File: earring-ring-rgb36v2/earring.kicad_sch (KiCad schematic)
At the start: 54 parts, among them J1 Conn_01x05, Q1 AO3401A, SW1 SW_Push, U2 STM32L031G6Ux

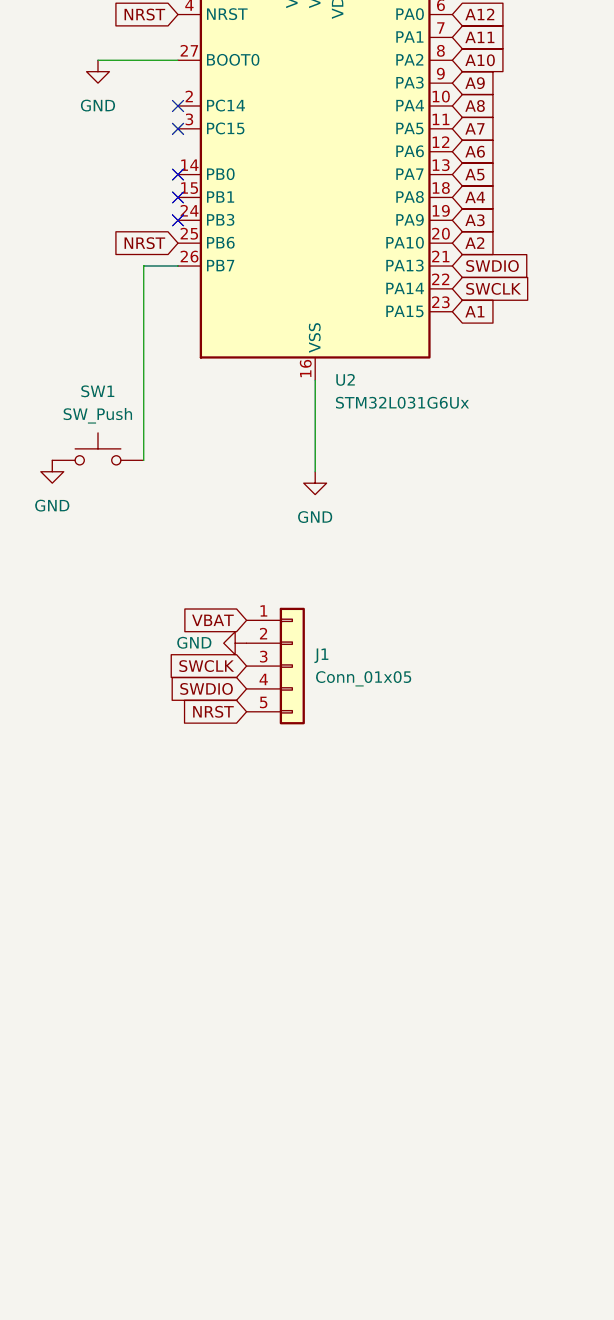
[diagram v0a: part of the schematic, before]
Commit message: earring-ring-rgb36v2: add phototransistor for light sensing
Can also be used for sending new programs, perhaps?
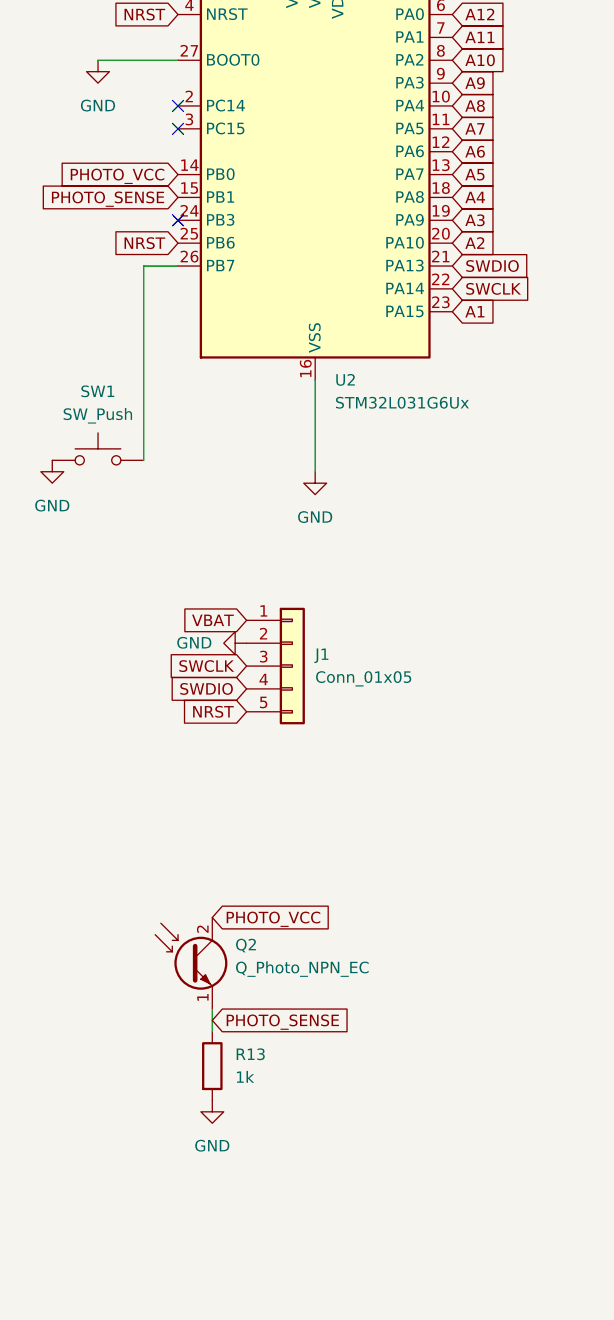
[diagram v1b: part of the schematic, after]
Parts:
- added Q2: Q_Photo_NPN_EC, Custom:Phototransistor_0603, symbol Device:Q_Photo_NPN_EC
- added R13: 1k, Resistor_SMD:R_0402_1005Metric, symbol Device:R
- J1: now left out of the parts list
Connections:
- net GND: now also R13.2
- net PHOTO_VCC: now reaches U2.14 (PB0)
- net PHOTO_VCC: now also Q2.2 (C)
- net PHOTO_SENSE: now reaches U2.15 (PB1)
- net PHOTO_SENSE: now also Q2.1 (E), R13.1
- no-connect marks 5 -> 3

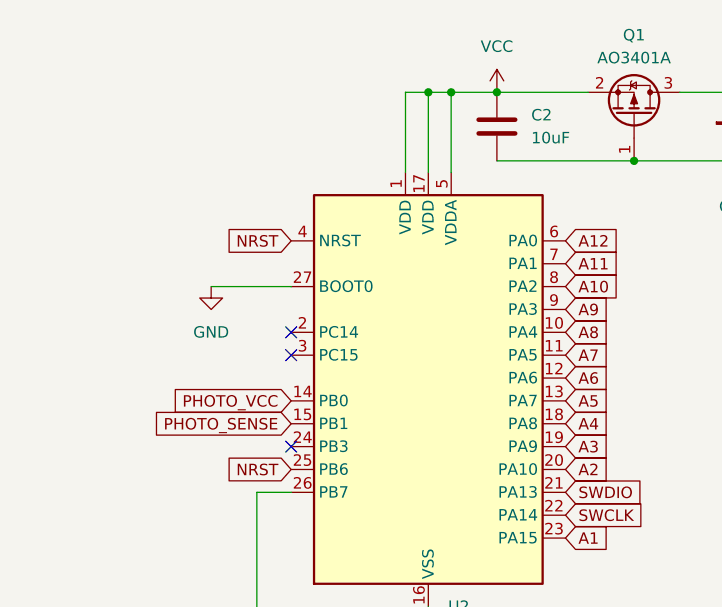
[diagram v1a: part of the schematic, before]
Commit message: earring-ring-rgb36v2: add 32768Hz crystal oscillator
No idea whether this is correct, might need some additional checking.
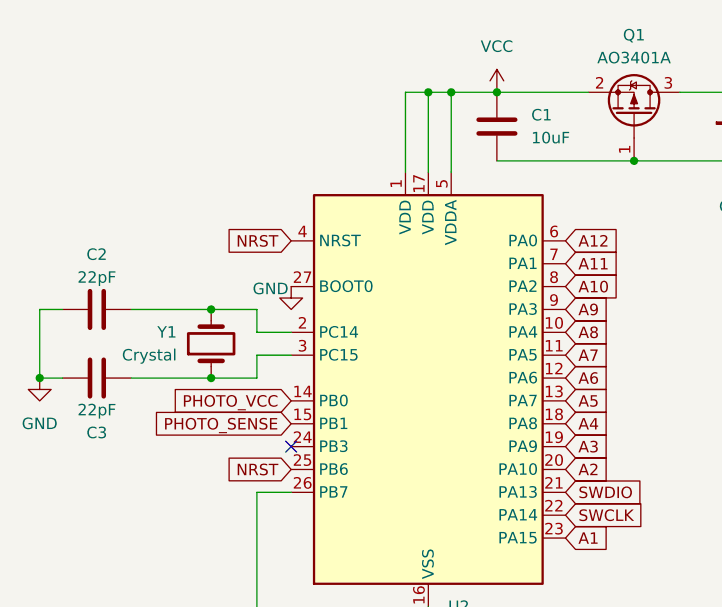
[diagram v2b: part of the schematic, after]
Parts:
- added C2, C3: 22pF, Capacitor_SMD:C_0402_1005Metric, symbol Device:C
- added Y1: Crystal, Crystal:Crystal_SMD_3215-2Pin_3.2x1.5mm, symbol Device:Crystal
- renumbered C2 to C1
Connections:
- net GND: now also C2.1, C3.1
- net at U2.2 (PC14): now also C2.2, Y1.2
- net at U2.3 (PC15): now also C3.2, Y1.1
- no-connect marks 3 -> 1
